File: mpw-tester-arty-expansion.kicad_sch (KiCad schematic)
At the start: 110 parts, among them J1 USB4105-GF-A, J10 61300211121, J11 61300211121, J12 61300211121, J14 61300311121, J15 61300311121, J18 61300411121, J19 61300711121, J2 61300211121, J20 61300411121, J3 Arty_A7_SPI, J4 61300211121, J5 61300311121, J6 61300211121, J7 61300211121, J8 61300211121, J9 61300211121, Q1 DTC014TEBTL, U1 SN74LVC1G125DCKR, U2 FT232HQ, U3 SN74LVC1G125DCKR, U4 MAX811REUS+T, U5 NTS0102DP, U6 MCP4661-103E/ML, U7 Caravel_breakout_PCB, U8 W25Q32FVSS, U9 MIC2211-AAYML-TR, Y1 ABM8G-12.000MHZ-18-D2Y-T, Y2 ECS-2520MVLC-100-BN-TR

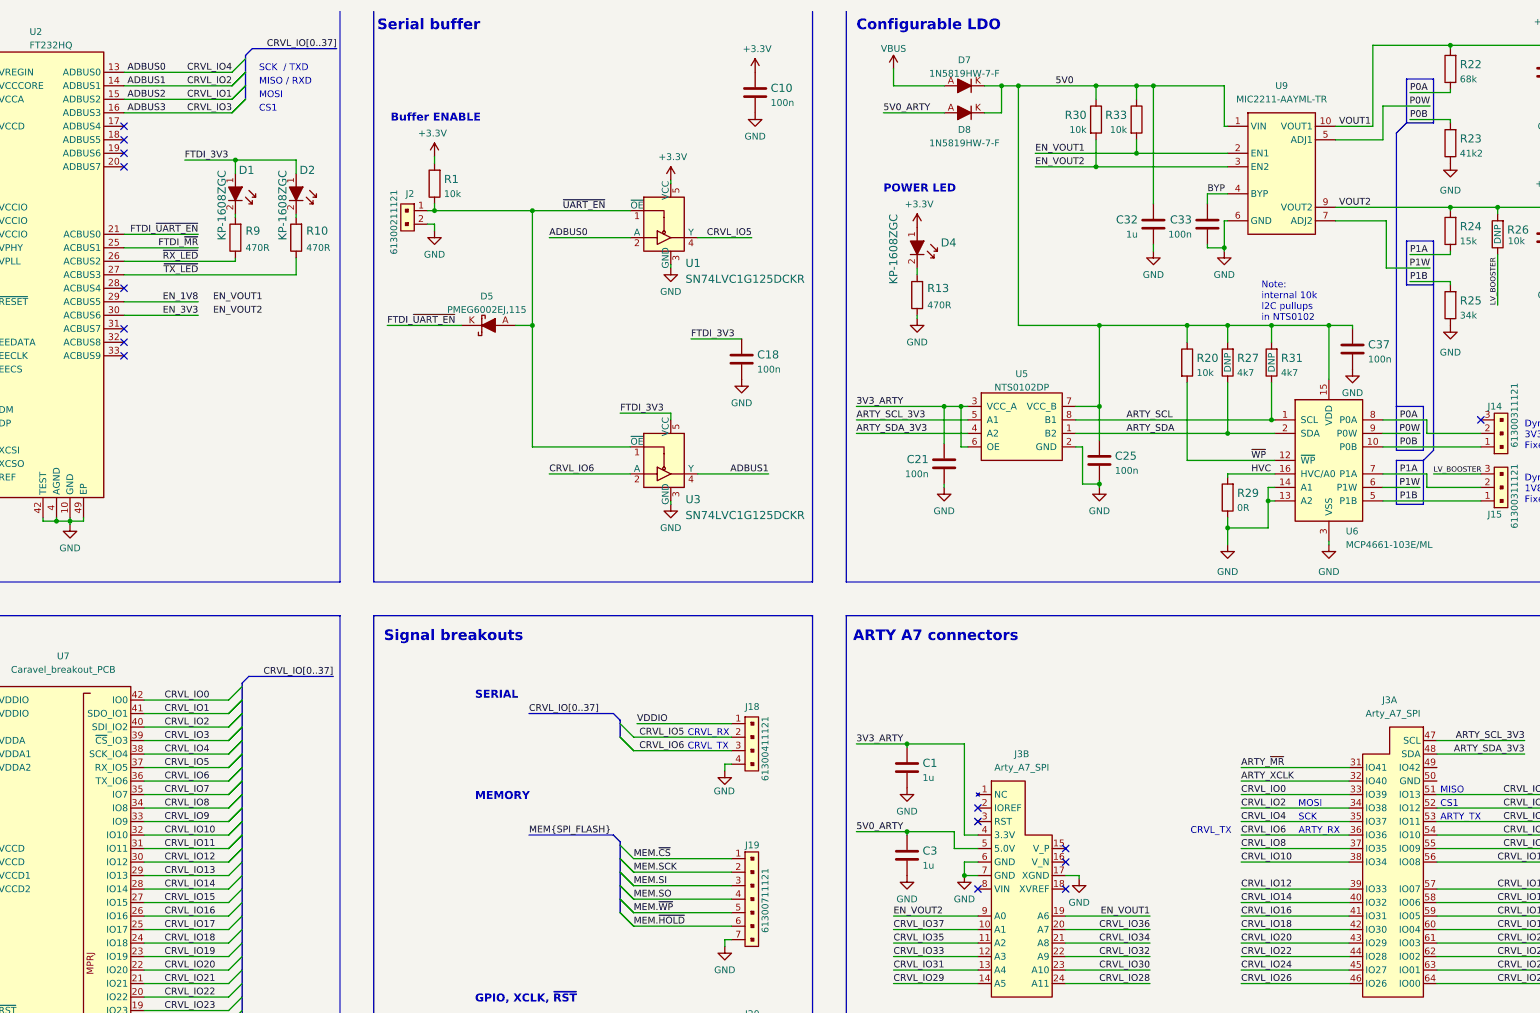
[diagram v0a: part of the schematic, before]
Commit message: Add LDO EN signals switch between ARTY and FTDI
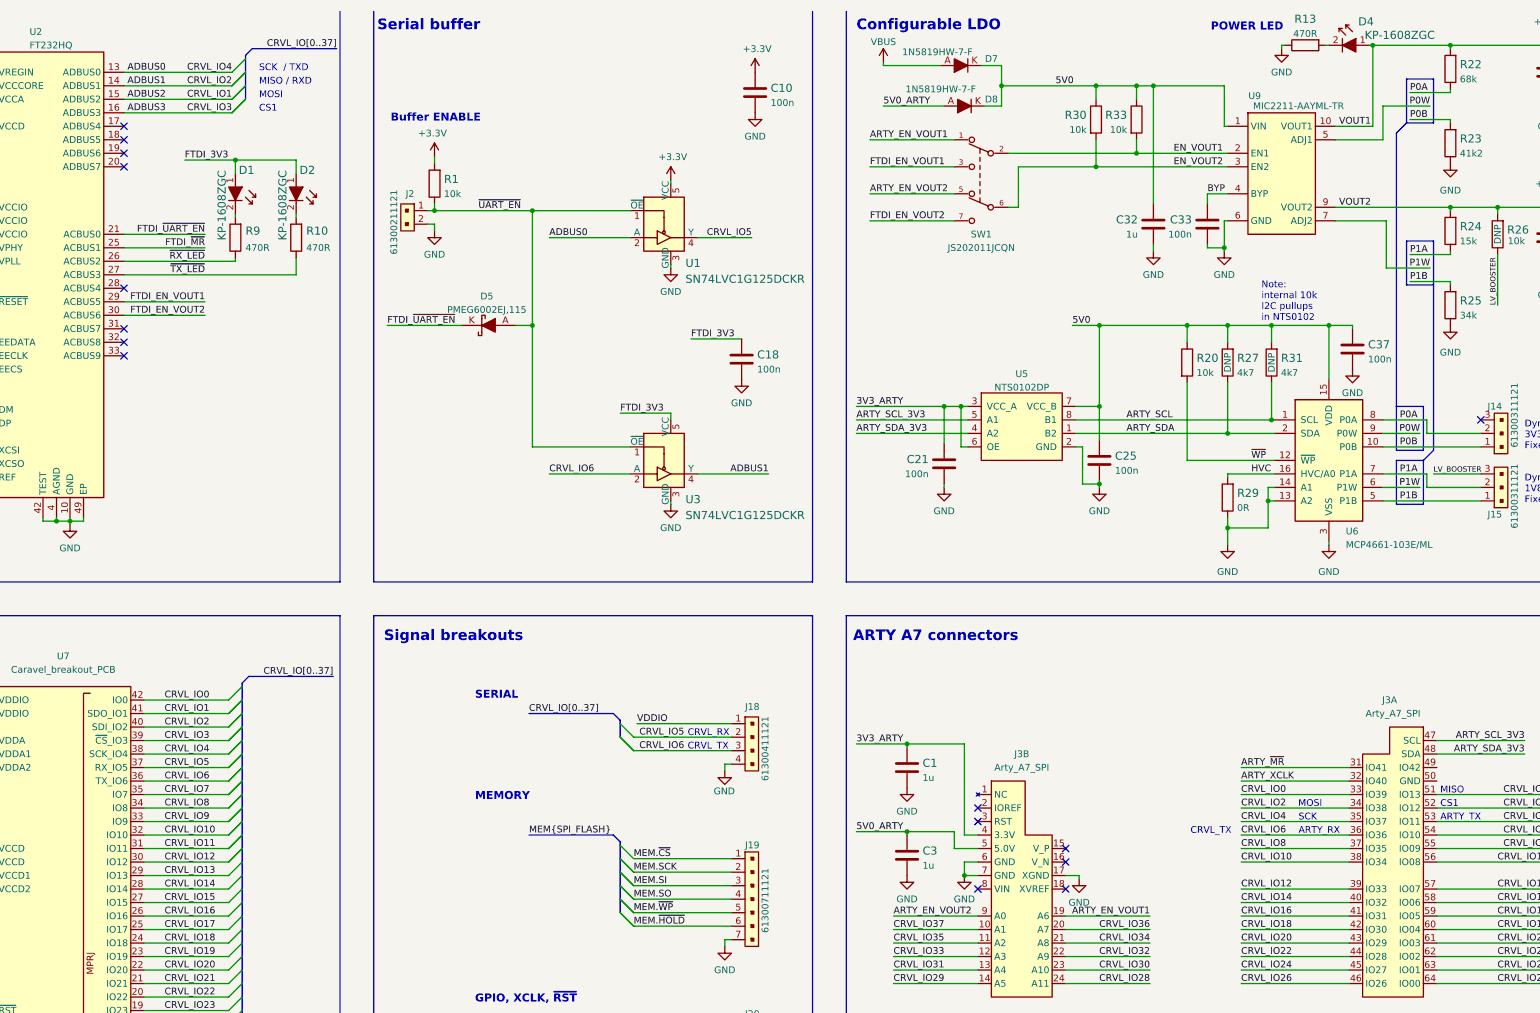
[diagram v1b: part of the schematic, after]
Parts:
- added SW1: JS202011JCQN, antmicro-footprints:JS202011JCQN, symbol antmicroSlideSwitches:JS202011JCQN
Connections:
- net EN_VOUT1: now also SW1.2 (1_C); no longer J3.19 (A6)
- net EN_VOUT2: now also SW1.6 (2_C); no longer J3.9 (A0)
- net EN_1V8 renamed FTDI_EN_VOUT1
- net FTDI_EN_VOUT1: now also SW1.3
- net EN_3V3 renamed FTDI_EN_VOUT2
- net FTDI_EN_VOUT2: now also SW1.7
- new net ARTY_EN_VOUT1: J3.19 (A6), SW1.1
- new net ARTY_EN_VOUT2: J3.9 (A0), SW1.5
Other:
- moved on the sheet: D4, D7, D8, R13

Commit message: correct too small footprint of FTDI, reconnect nearby tracks
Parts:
- U2: footprint antmicro-footprints:QFN-48-1EP_6x6mm -> antmicro-footprints:QFN-48-1EP_7x7mm
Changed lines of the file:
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@@
     (rev "0.0.99")
   )
-  (bus_alias "SPI_FLASH" (members "~{CS}" "SCK" "SI" "SO" "~{WP}" "~{HOLD}"))
   (bus_alias "SPI" (members "~{CS}" "MISO" "MOSI" "SCK"))
+  (bus_alias "SPI_FLASH" (members "~{CS}" "SCK" "SI" "SO" "~{WP}" "~{HOLD}"))
   (junction (at 313.69 42.545) (diameter 0) (color 0 0 0 0)
   )
@@
       (effects (font (size 1.27 1.27)) (justify left))
     )
-    (property "Footprint" "antmicro-footprints:QFN-48-1EP_6x6mm" (id 2) (at 118.745 111.76 0)
+    (property "Footprint" "antmicro-footprints:QFN-48-1EP_7x7mm" (id 2) (at 118.745 111.76 0)
       (effects (font (size 1.27 1.27)) hide)
     )
@@
     )
     (path "/a0c2fa84-fc21-44d2-8ce1-fce5d439b224"
-      (reference "U2") (unit 1) (value "FT232HQ") (footprint "antmicro-footprints:QFN-48-1EP_6x6mm")
+      (reference "U2") (unit 1) (value "FT232HQ") (footprint "antmicro-footprints:QFN-48-1EP_7x7mm")
     )
     (path "/e502d386-c8b8-460b-bee6-05a8179e5cc1"

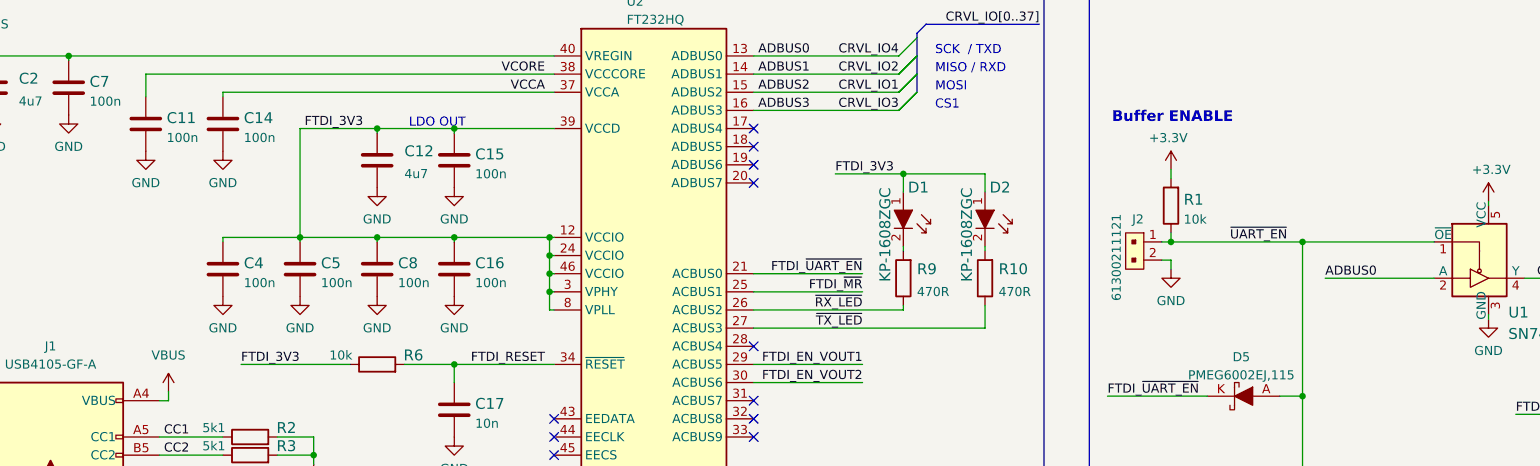
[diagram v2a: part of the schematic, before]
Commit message: Update FT232H footprint
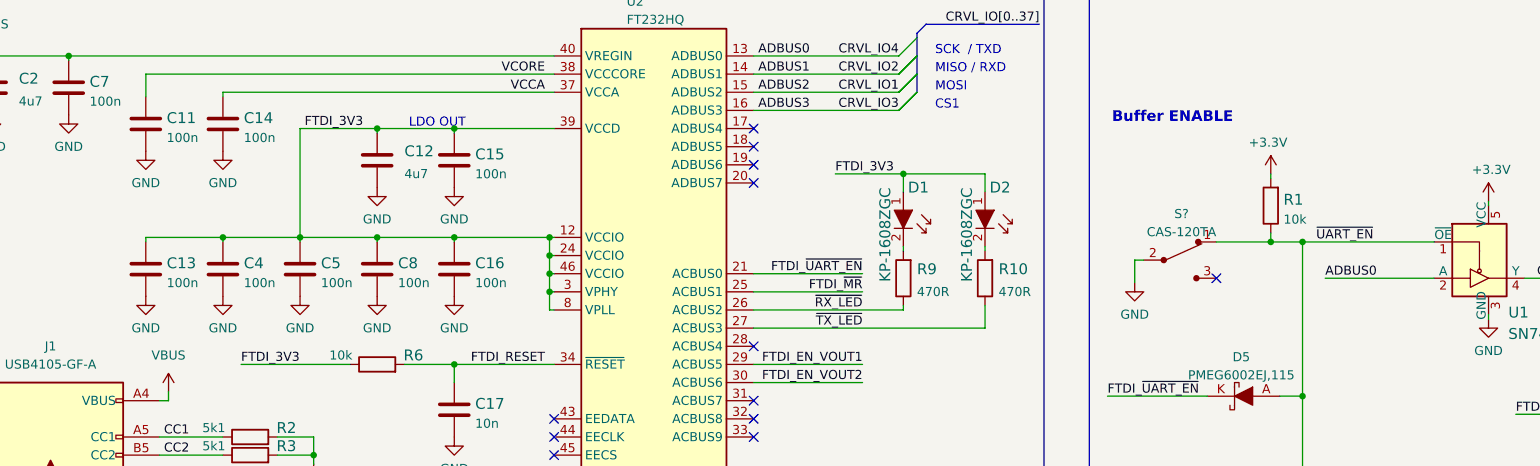
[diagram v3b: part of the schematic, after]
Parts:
- removed J2: 61300211121, antmicro-footprints:PinHeader_1x2_P2.54_Drill0.9mm, symbol antmicroRectangularConnectorsHeadersMalePins:61300211121
- added C13: C_100n_0603, antmicro-footprints:0603-cap, symbol antmicroCapacitors0603:C_100n_0603
- added S?: CAS-120TA, antmicro-footprints:Switch_Slide_CAS-120TA, symbol antmicroSlideSwitches:CAS-120TA
- U2: footprint antmicro-footprints:QFN-48-1EP_7x7mm -> antmicro-footprints:QFN-48-1EP_8x8mm_P0.5mm_EP6.2x6.2mm_FT232HQ_marking
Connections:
- net AGND: now also C13.2, S?.2
- net FTDI_3V3: now also C13.1
- net ~{UART_EN}: now also S?.1
- no-connect marks 21 -> 22
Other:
- moved on the sheet: R1
